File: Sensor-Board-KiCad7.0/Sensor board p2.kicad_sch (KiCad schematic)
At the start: 44 parts, among them Q1 SMMBFJ177LT1G, Q2 SMMBFJ177LT1G, Q3 SMMBFJ177LT1G, U14 PS1-NO2-50, U15 PS1-CO-1000, U16 LMV721, U17 LMV721, U18 LMV721, U19 PS1-SO2-50, U21 LMV721, U22 LMV721, U23 OPAMP, U24 BME680, U25 NAU7802_24-bit_ADC, U26 NAU7802_24-bit_ADC

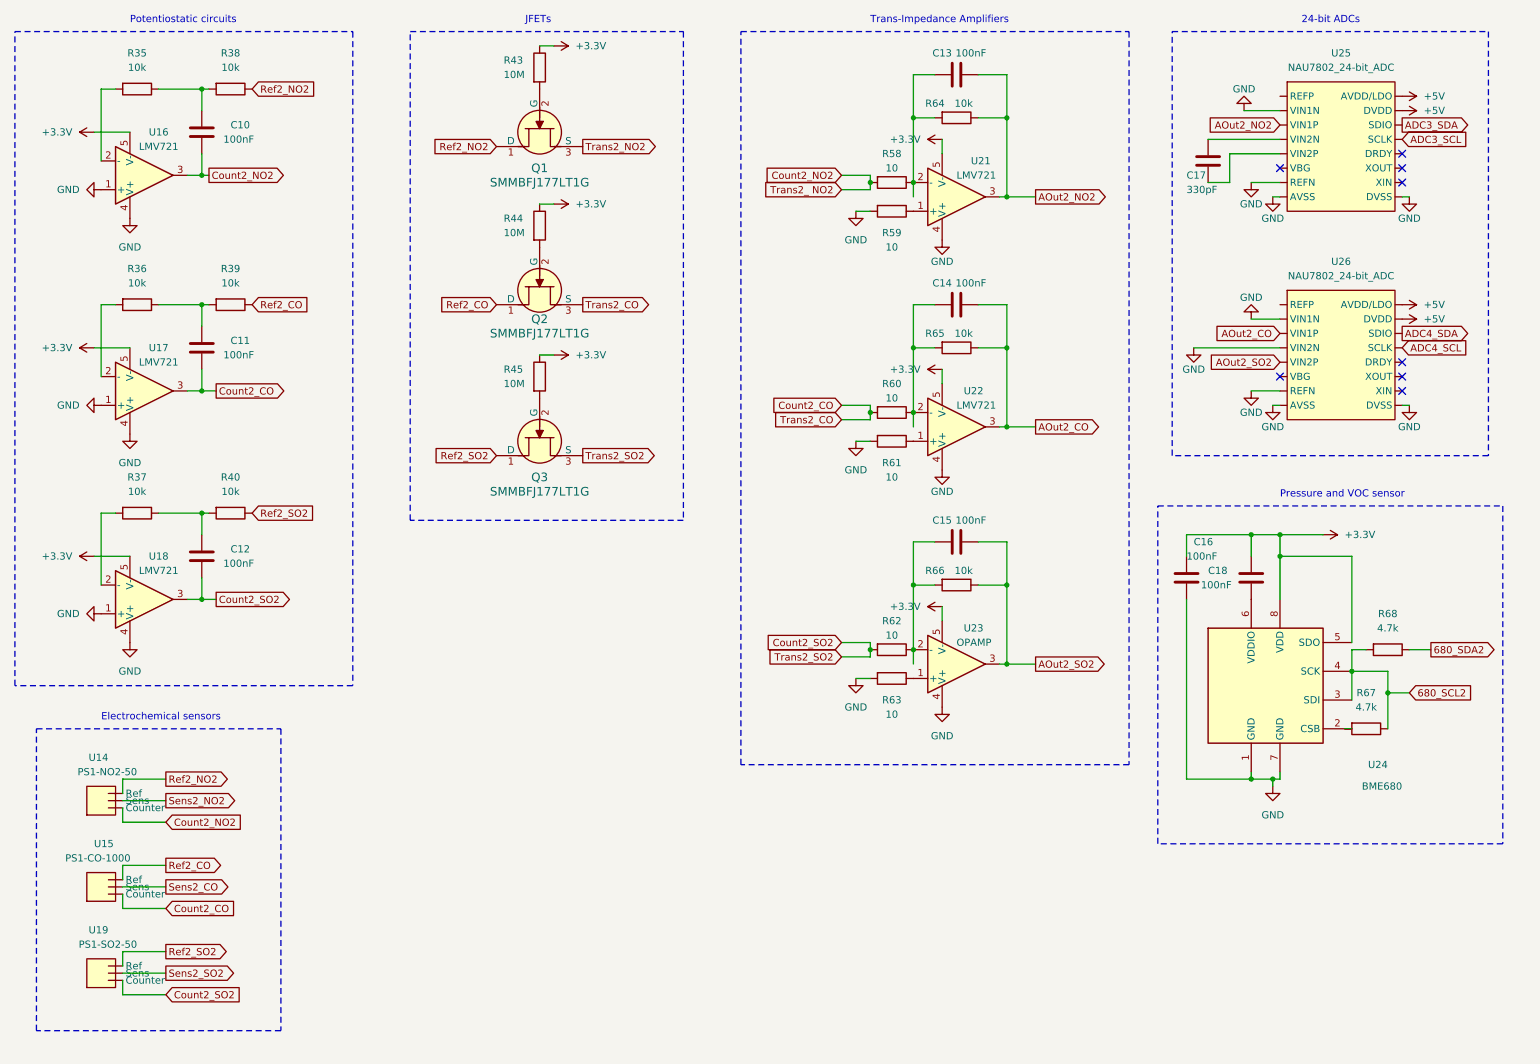
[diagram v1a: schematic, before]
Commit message: Added test points to I2C
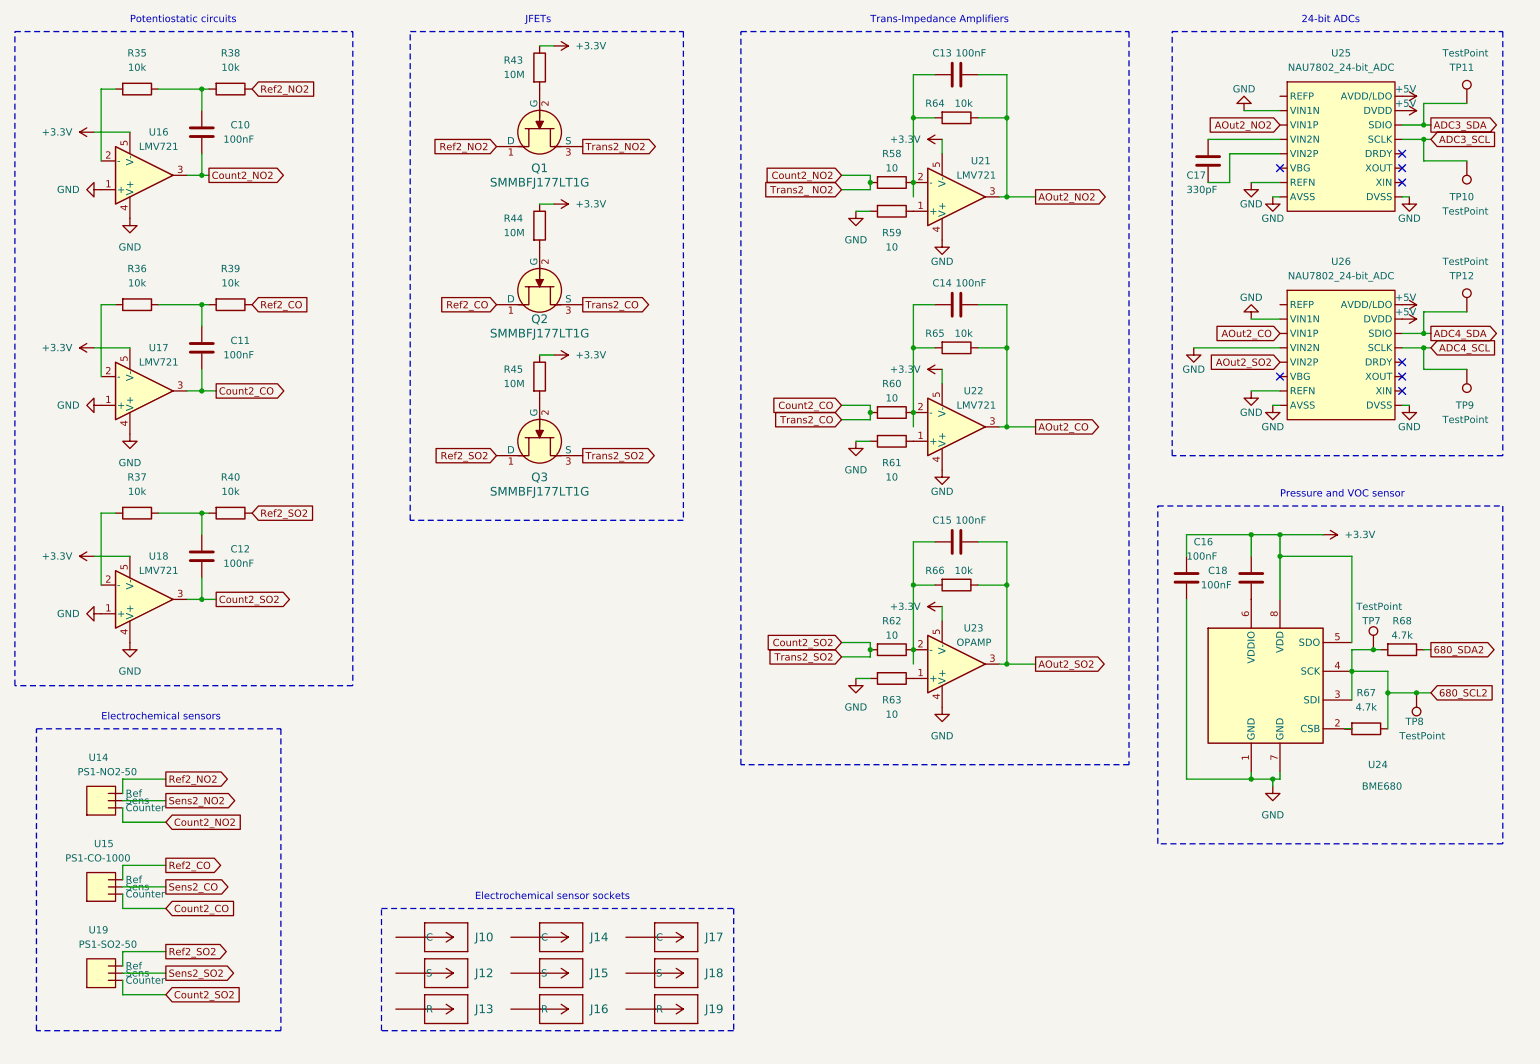
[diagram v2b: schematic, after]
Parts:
- added J10, J12, J13, J14, J15, J16, J17, J18, J19: 9401-0-15-15-23-27-10-0, CONN_0384-0-67-80-23-27-10-0_MIM, symbol EChem Socket:9401-0-15-15-23-27-10-0
- added TP10, TP11, TP12, TP7, TP8, TP9: TestPoint, symbol Connector:TestPoint
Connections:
- net 680_SCL2: now also TP7.1, TP8.1
- net ADC3_SCL: now also TP10.1
- net ADC3_SDA: now also TP11.1
- net ADC4_SCL: now also TP9.1
- net ADC4_SDA: now also TP12.1
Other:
- note added: "Electrochemical sensor sockets"
- moved on the sheet: R68

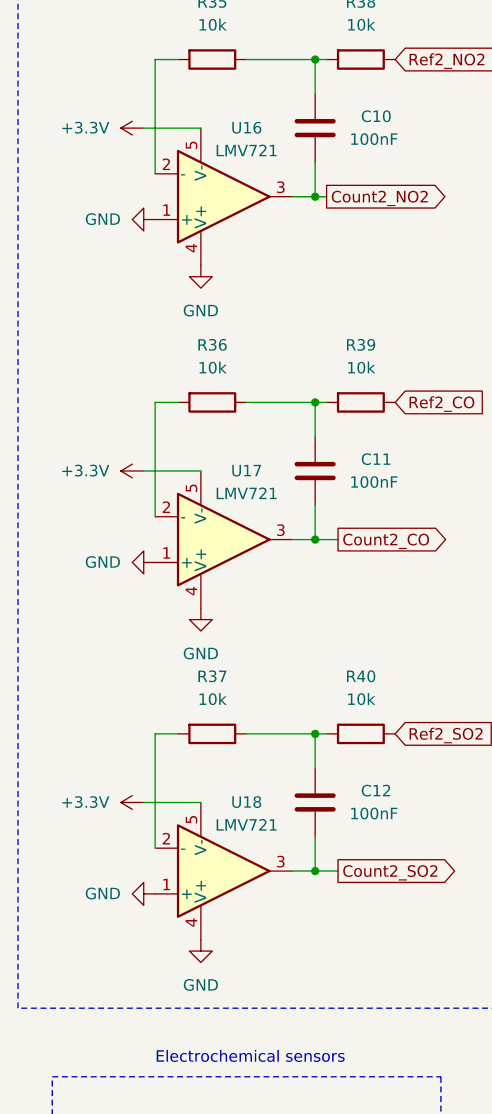
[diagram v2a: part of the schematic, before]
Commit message: Added resistors and changed JFEt
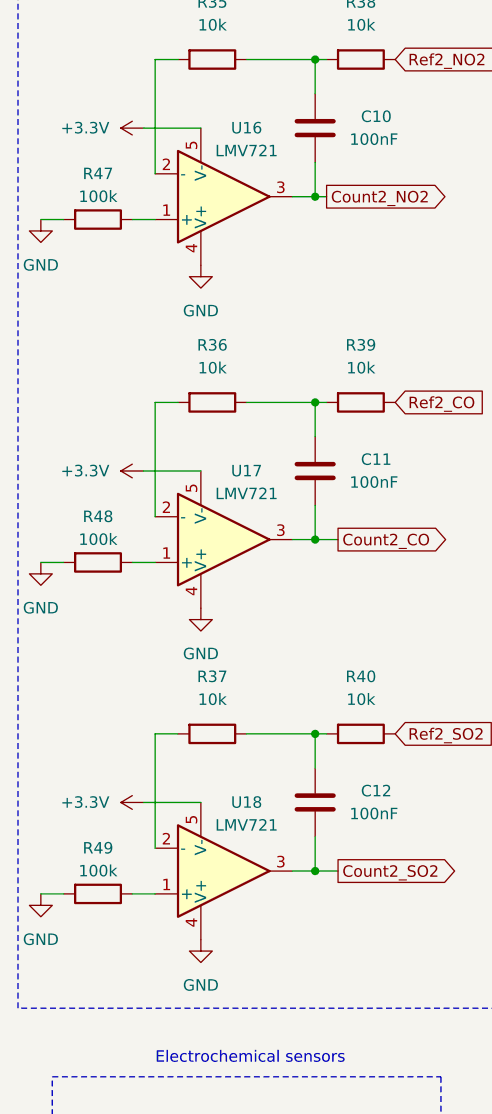
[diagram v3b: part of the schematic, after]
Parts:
- added R47, R48, R49: 100k, symbol Device:R
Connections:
- net GND: now also R47.2, R48.2, R49.2; no longer U16.1 (+), U17.1 (+), U18.1 (+)
- new net: R48.1, U17.1 (+)
- new net: R49.1, U18.1 (+)
- new net: R47.1, U16.1 (+)
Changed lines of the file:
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@@
+    (stroke (width 0) (type default))
+  )
+  (wire (pts (xy 17.78 119.38) (xy 20.32 119.38))
     (stroke (width 0) (type default))
   )
@@
     (stroke (width 0) (type default))
   )
+  (wire (pts (xy 27.94 82.55) (xy 30.48 82.55))
+    (stroke (width 0) (type default))
+  )
   (wire (pts (xy 34.29 152.4) (xy 41.91 152.4))
     (stroke (width 0) (type default))
@@
     (stroke (width 0) (type default))
   )
+  (wire (pts (xy 27.94 44.45) (xy 30.48 44.45))
+    (stroke (width 0) (type default))
+  )
   (wire (pts (xy 237.49 148.59) (xy 237.49 149.86))
     (stroke (width 0) (type default))
@@
     (stroke (width 0) (type default))
   )
+  (wire (pts (xy 17.78 82.55) (xy 20.32 82.55))
+    (stroke (width 0) (type default))
+  )
   (wire (pts (xy 179.07 120.65) (xy 179.07 118.11))
     (stroke (width 0) (type default))
@@
     (stroke (width 0) (type default))
   )
+  (wire (pts (xy 27.94 119.38) (xy 30.48 119.38))
+    (stroke (width 0) (type default))
+  )
   (wire (pts (xy 48.26 64.77) (xy 48.26 68.58))
     (stroke (width 0) (type default))
@@
   )
   (wire (pts (xy 177.8 24.13) (xy 173.99 24.13))
+    (stroke (width 0) (type default))
+  )
+  (wire (pts (xy 17.78 44.45) (xy 20.32 44.45))
     (stroke (width 0) (type default))
   )
@@
     )
   )
-  (symbol (lib_id "power:GND") (at 30.48 44.45 270) (unit 1)
-    (in_bom yes) (on_board yes) (dnp no) (fields_autoplaced)
-    (property "Reference" "#PWR09" (at 24.13 44.45 0)
-      (effects (font (size 1.27 1.27)) hide)
-    )
-    (property "Value" "GND" (at 26.67 44.4499 90)
-      (effects (font (size 1.27 1.27)) (justify right))
-    )
-    (property "Footprint" "" (at 30.48 44.45 0)
-      (effects (font (size 1.27 1.27)) hide)
-    )
-    (property "Datasheet" "" (at 30.48 44.45 0)
+  (symbol (lib_id "power:GND") (at 17.78 44.45 0) (unit 1)
+    (in_bom yes) (on_board yes) (dnp no) (fields_autoplaced)
+    (property "Reference" "#PWR09" (at 17.78 50.8 0)
+      (effects (font (size 1.27 1.27)) hide)
+    )
+    (property "Value" "GND" (at 17.78 49.53 0)
+      (effects (font (size 1.27 1.27)))
+    )
+    (property "Footprint" "" (at 17.78 44.45 0)
+      (effects (font (size 1.27 1.27)) hide)
+    )
+    (property "Datasheet" "" (at 17.78 44.45 0)
       (effects (font (size 1.27 1.27)) hide)
     )
@@
         (path "/3a986dcd-349f-492d-950a-09832b2e5abd/eb03ba60-66c2-4345-a3c2-908f0a643e89"
           (reference "#PWR031") (unit 1)
+        )
+      )
+    )
+  )
+  (symbol (lib_id "Device:R") (at 24.13 82.55 270) (unit 1)
+    (in_bom yes) (on_board yes) (dnp no)
+    (property "Reference" "R48" (at 24.13 77.47 90)
+      (effects (font (size 1.27 1.27)))
+    )
+    (property "Value" "100k" (at 24.13 80.01 90)
+      (effects (font (size 1.27 1.27)))
+    )
+    (property "Footprint" "" (at 24.13 80.772 90)
+      (effects (font (size 1.27 1.27)) hide)
+    )
+    (property "Datasheet" "~" (at 24.13 82.55 0)
+      (effects (font (size 1.27 1.27)) hide)
+    )
+    (pin "2")
+    (pin "1")
+    (instances
+      (project "Sensor-Board"
+        (path "/3a986dcd-349f-492d-950a-09832b2e5abd/eb03ba60-66c2-4345-a3c2-908f0a643e89"
+          (reference "R48") (unit 1)
         )
       )
@@
     )
   )
+  (symbol (lib_id "Device:R") (at 24.13 119.38 270) (unit 1)
+    (in_bom yes) (on_board yes) (dnp no)
+    (property "Reference" "R49" (at 24.13 114.3 90)
+      (effects (font (size 1.27 1.27)))
+    )
+    (property "Value" "100k" (at 24.13 116.84 90)
+      (effects (font (size 1.27 1.27)))
+    )
+    (property "Footprint" "" (at 24.13 117.602 90)
+      (effects (font (size 1.27 1.27)) hide)
+    )
+    (property "Datasheet" "~" (at 24.13 119.38 0)
+      (effects (font (size 1.27 1.27)) hide)
+    )
+    (pin "2")
+    (pin "1")
+    (instances
+      (project "Sensor-Board"
+        (path "/3a986dcd-349f-492d-950a-09832b2e5abd/eb03ba60-66c2-4345-a3c2-908f0a643e89"
+          (reference "R49") (unit 1)
+        )
+      )
+    )
+  )
   (symbol (lib_id "power:GND") (at 179.07 93.98 0) (unit 1)
     (in_bom yes) (on_board yes) (dnp no)
@@
     )
   )
-  (symbol (lib_id "power:GND") (at 30.48 82.55 270) (unit 1)
-    (in_bom yes) (on_board yes) (dnp no) (fields_autoplaced)
-    (property "Reference" "#PWR010" (at 24.13 82.55 0)
-      (effects (font (size 1.27 1.27)) hide)
-    )
-    (property "Value" "GND" (at 26.67 82.5499 90)
-      (effects (font (size 1.27 1.27)) (justify right))
-    )
-    (property "Footprint" "" (at 30.48 82.55 0)
-      (effects (font (size 1.27 1.27)) hide)
-    )
-    (property "Datasheet" "" (at 30.48 82.55 0)
+  (symbol (lib_id "power:GND") (at 17.78 82.55 0) (unit 1)
+    (in_bom yes) (on_board yes) (dnp no) (fields_autoplaced)
+    (property "Reference" "#PWR010" (at 17.78 88.9 0)
+      (effects (font (size 1.27 1.27)) hide)
+    )
+    (property "Value" "GND" (at 17.78 87.63 0)
+      (effects (font (size 1.27 1.27)))
+    )
+    (property "Footprint" "" (at 17.78 82.55 0)
+      (effects (font (size 1.27 1.27)) hide)
+    )
+    (property "Datasheet" "" (at 17.78 82.55 0)
       (effects (font (size 1.27 1.27)) hide)
     )
@@
     )
   )
-  (symbol (lib_id "power:GND") (at 30.48 119.38 270) (unit 1)
-    (in_bom yes) (on_board yes) (dnp no) (fields_autoplaced)
-    (property "Reference" "#PWR011" (at 24.13 119.38 0)
-      (effects (font (size 1.27 1.27)) hide)
-    )
-    (property "Value" "GND" (at 26.67 119.3799 90)
-      (effects (font (size 1.27 1.27)) (justify right))
-    )
-    (property "Footprint" "" (at 30.48 119.38 0)
-      (effects (font (size 1.27 1.27)) hide)
-    )
-    (property "Datasheet" "" (at 30.48 119.38 0)
+  (symbol (lib_id "power:GND") (at 17.78 119.38 0) (unit 1)
+    (in_bom yes) (on_board yes) (dnp no) (fields_autoplaced)
+    (property "Reference" "#PWR011" (at 17.78 125.73 0)
+      (effects (font (size 1.27 1.27)) hide)
+    )
+    (property "Value" "GND" (at 17.78 124.46 0)
+      (effects (font (size 1.27 1.27)))
+    )
+    (property "Footprint" "" (at 17.78 119.38 0)
+      (effects (font (size 1.27 1.27)) hide)
+    )
+    (property "Datasheet" "" (at 17.78 119.38 0)
       (effects (font (size 1.27 1.27)) hide)
     )
@@
         )
       )
+    )
+  )
+  (symbol (lib_id "Device:R") (at 24.13 44.45 270) (unit 1)
+    (in_bom yes) (on_board yes) (dnp no)
+    (property "Reference" "R47" (at 24.13 39.37 90)
+      (effects (font (size 1.27 1.27)))
+    )
+    (property "Value" "100k" (at 24.13 41.91 90)
+      (effects (font (size 1.27 1.27)))
+    )
+    (property "Footprint" "" (at 24.13 42.672 90)
+      (effects (font (size 1.27 1.27)) hide)
+    )
+    (property "Datasheet" "~" (at 24.13 44.45 0)
+      (effects (font (size 1.27 1.27)) hide)
+    )
+    (pin "2")
+    (pin "1")
+    (instances
+      (project "Sensor-Board"
+        (path "/3a986dcd-349f-492d-950a-09832b2e5abd/eb03ba60-66c2-4345-a3c2-908f0a643e89"
+          (reference "R47") (unit 1)
+        )
+      )

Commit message: Saved
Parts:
- removed Q1, Q2, Q3: SMMBFJ177LT1G, digikey-footprints:TO-92-3_Formed_Leads, symbol dk_Transistors-JFETs:J175-D26Z
- added U29, U30, U31: MMBFJ177LT1G, SOT_77LT1G_ONS, symbol MMBFJ177LT1-D:MMBFJ177LT1G
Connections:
- net Count2_CO: now also U30.2 (S)
- net Count2_SO2: now also U31.2 (S)
- net Ref2_CO: now also U30.3 (D)
- net Ref2_NO2: now also U29.3 (D)
- net Ref2_SO2: now also U31.3 (D)
- net Trans2_NO2: now also U29.2 (S)
- net at R44.2: now also U30.1 (G)
- net at R45.2: now also U31.1 (G)
- net at R43.2: now also U29.1 (G)
